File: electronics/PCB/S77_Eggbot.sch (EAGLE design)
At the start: 21 parts, among them U1 CR_LM2596, U2 S2_MINI, U3 CARRIER_A4988, U4 CARRIER_A4988, X1 PWR, X2 B6B-PH, X3 B6B-PH

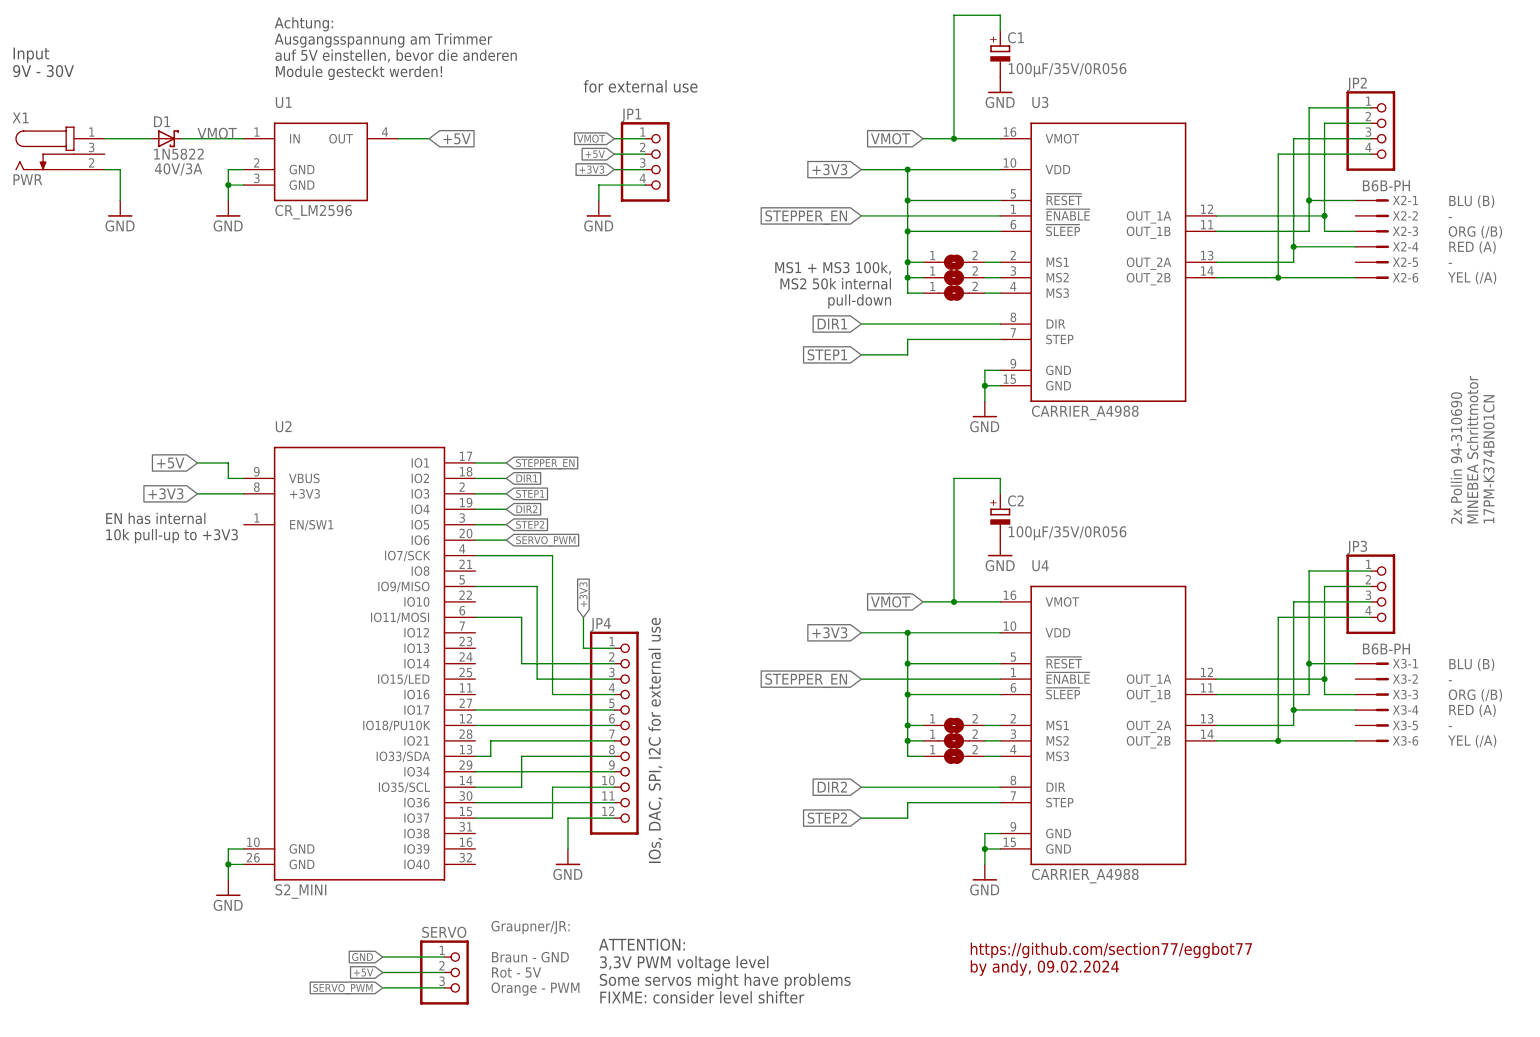
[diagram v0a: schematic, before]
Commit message: PCB: added 3.3V<->5V levelshifter for servo PWM, update exports
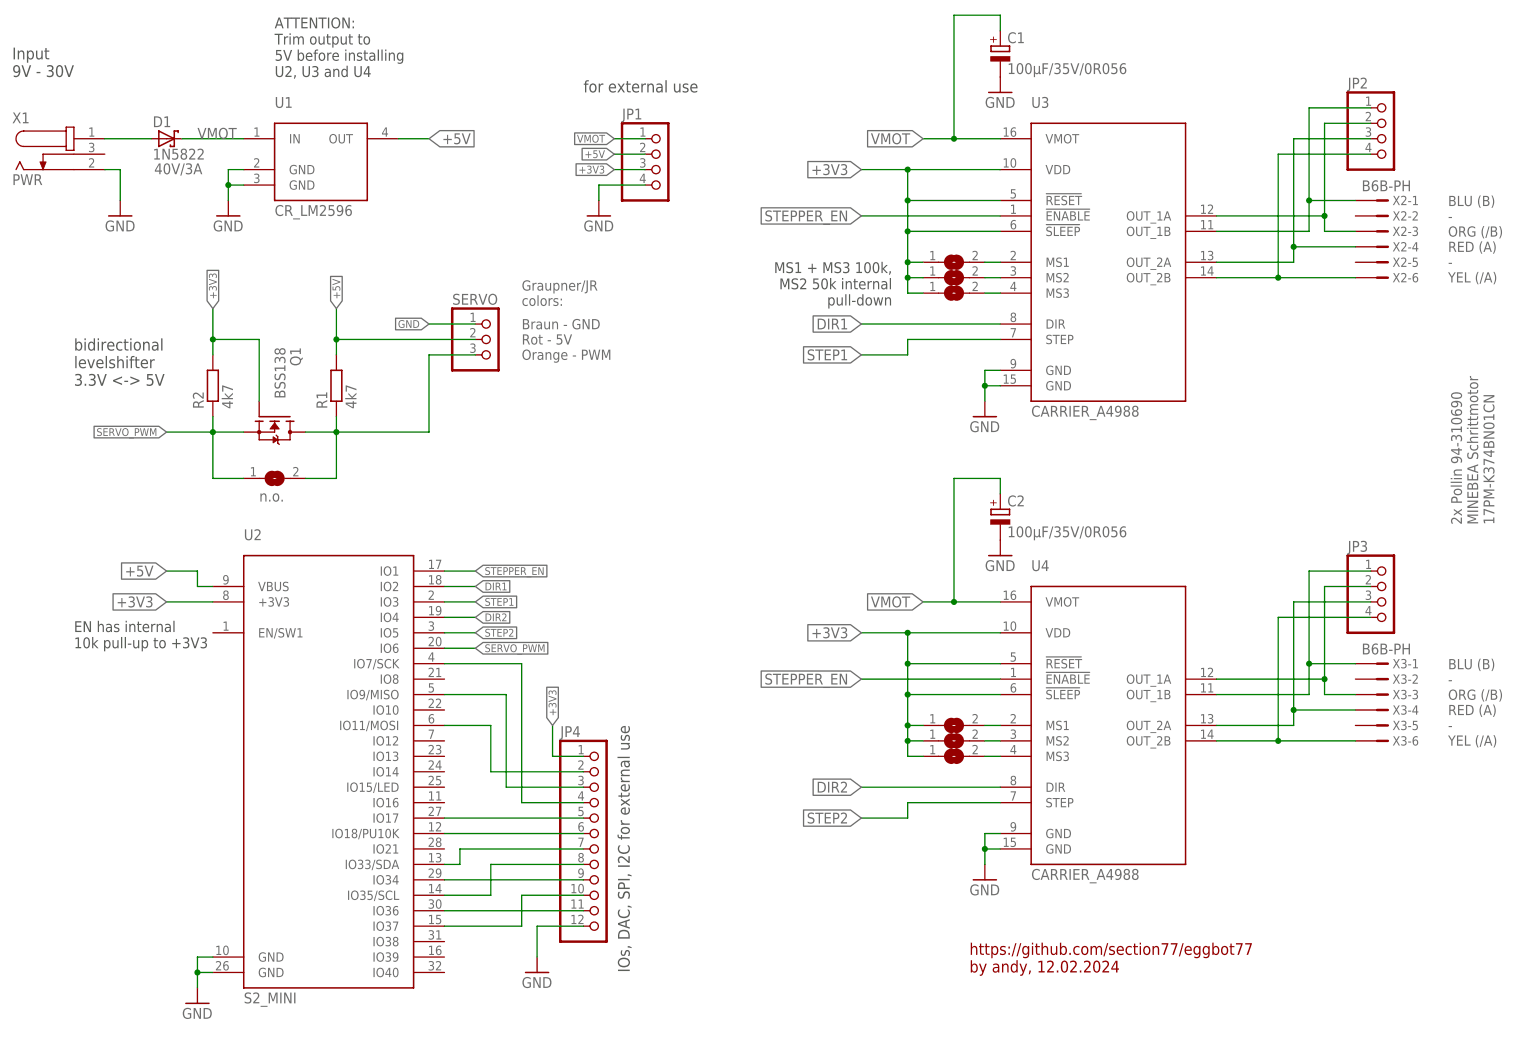
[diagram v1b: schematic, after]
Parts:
- added Q1: BSS138, bss138_10:BSS138
- added R1, R2: 4k7, rcl:R-EU_R1206
- added SJ7: n.o., jumper:SJ
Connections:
- new net N$1: Q1.D, R1.1, SERVO.3, SJ7.2
- net +3V3: now also Q1.G, R2.2
- net +5V: now also R1.2
- net SERVO_PWM: now also Q1.S, R2.1, SJ7.1; no longer SERVO.3
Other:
- note added: "ATTENTION: Trim output to 5V before installing U2, U3 and U4"
- note added: "Graupner/JR colors:"
- note added: "bidirectional levelshifter 3.3V <-> 5V"
- note added: "https://github.com/section77/eggbot77 by andy, 12.02.2024"
- note removed: "ATTENTION: 3,3V PWM voltage level Some servos might have problems FIXME: consider level shifter"
- note removed: "Achtung: Ausgangsspannung am Trimmer auf 5V einstellen, bevor die anderen Module gesteckt werden!"
- note removed: "Graupner/JR:"
- note removed: "https://github.com/section77/eggbot77 by andy, 09.02.2024"
- moved on the sheet: JP4, SERVO, U2
